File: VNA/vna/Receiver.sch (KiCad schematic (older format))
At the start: 13 parts, among them U5 AD8302ARUZ

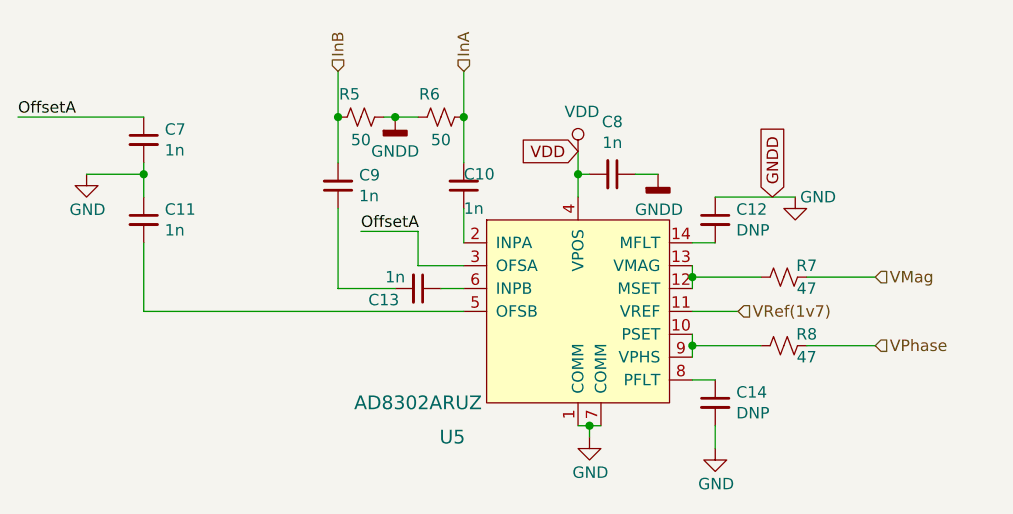
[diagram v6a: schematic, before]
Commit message: initial pcb design
initial layout and grouping of components complete
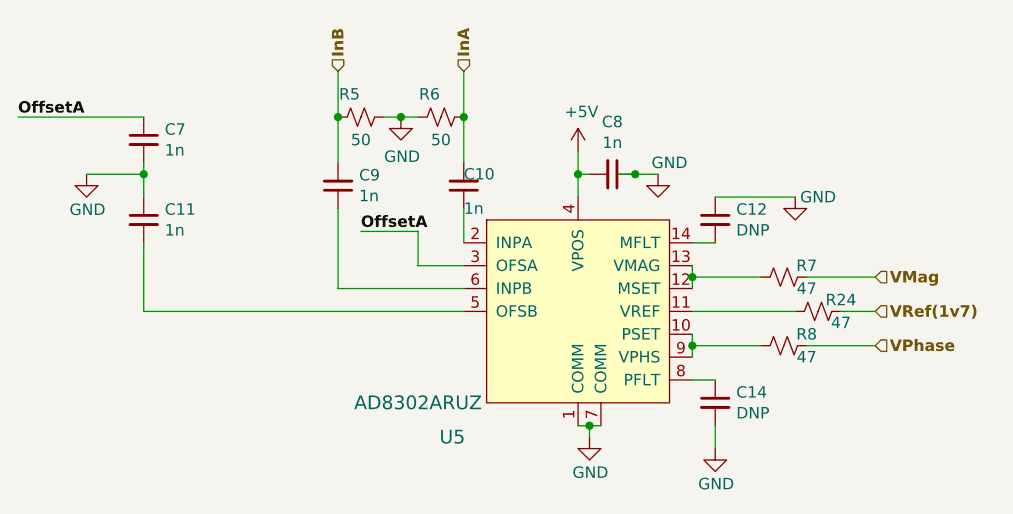
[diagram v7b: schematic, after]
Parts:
- removed C13: 1n, Capacitor_SMD:C_1206_3216Metric_Pad1.42x1.75mm_HandSolder, symbol Device:C_Small
- added R24: 47, Resistor_SMD:R_0805_2012Metric_Pad1.15x1.40mm_HandSolder, symbol Device:R_Small_US
- C10, C11, C12, C14, C7, C8, C9: footprint Capacitor_SMD:C_1206_3216Metric_Pad1.42x1.75mm_HandSolder -> Capacitor_SMD:C_0805_2012Metric_Pad1.15x1.40mm_HandSolder
- R5, R6, R7, R8: footprint Resistor_SMD:R_1206_3216Metric_Pad1.42x1.75mm_HandSolder -> Resistor_SMD:R_0805_2012Metric_Pad1.15x1.40mm_HandSolder
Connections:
- net VRef(1v7): now also R24.1; no longer U5.11 (VREF)
- net at U5.6 (INPB): now also C9.1
- net VDD renamed +5V
- new net: R24.2, U5.11 (VREF)
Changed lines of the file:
@@
 $Descr A4 11693 8268
 encoding utf-8
-Sheet 6 10
-Title ""
-Date ""
-Rev ""
-Comp ""
+Sheet 5 10
+Title "Receiver"
+Date "2019-09-25"
+Rev "0.1"
+Comp "Benjamin Jackson"
 Comment1 ""
 Comment2 ""
@@
 F 0 "C12" H 6142 2796 50  0000 L CNN
 F 1 "DNP" H 6142 2705 50  0000 L CNN
-F 2 "Capacitor_SMD:C_1206_3216Metric_Pad1.42x1.75mm_HandSolder" H 6050 2750 50  0001 C CNN
+F 2 "Capacitor_SMD:C_0805_2012Metric_Pad1.15x1.40mm_HandSolder" H 6050 2750 50  0001 C CNN
 F 3 "~" H 6050 2750 50  0001 C CNN
 	1    6050 2750
@@
 F 0 "C14" H 6142 3596 50  0000 L CNN
 F 1 "DNP" H 6142 3505 50  0000 L CNN
-F 2 "Capacitor_SMD:C_1206_3216Metric_Pad1.42x1.75mm_HandSolder" H 6050 3550 50  0001 C CNN
+F 2 "Capacitor_SMD:C_0805_2012Metric_Pad1.15x1.40mm_HandSolder" H 6050 3550 50  0001 C CNN
 F 3 "~" H 6050 3550 50  0001 C CNN
 	1    6050 3550
@@
 F 0 "C10" H 4950 2550 50  0000 R CNN
 F 1 "1n" H 4950 2700 50  0000 R CNN
-F 2 "Capacitor_SMD:C_1206_3216Metric_Pad1.42x1.75mm_HandSolder" H 4950 2600 50  0001 C CNN
+F 2 "Capacitor_SMD:C_0805_2012Metric_Pad1.15x1.40mm_HandSolder" H 4950 2600 50  0001 C CNN
 F 3 "~" H 4950 2600 50  0001 C CNN
 	1    4950 2600
@@
 Wire Wire Line
 	5950 3450 6050 3450
-$Comp
-L Device:C_Small C13
-U 1 1 5CCC193D
-P 4750 3050
-F 0 "C13" V 4800 2900 50  0000 C CNN
-F 1 "1n" V 4700 2950 50  0000 C CNN
-F 2 "Capacitor_SMD:C_1206_3216Metric_Pad1.42x1.75mm_HandSolder" H 4750 3050 50  0001 C CNN
-F 3 "~" H 4750 3050 50  0001 C CNN
-	1    4750 3050
-	0    1    1    0
-$EndComp
 $Comp
 L power:GND #PWR023
@@
 Wire Wire Line
 	4950 2700 4950 2850
-Text HLabel 4950 2100 1    50   Input ~ 0
+Text HLabel 4950 2100 1    50   Input ~ 10
 InA
 Wire Wire Line
-	4850 3050 4950 3050
-Wire Wire Line
 	4950 2500 4950 2300
-$Comp
-L power:VDD #PWR019
-U 1 1 5CCC3643
-P 5450 2450
-F 0 "#PWR019" H 5450 2300 50  0001 C CNN
-F 1 "VDD" H 5467 2623 50  0000 C CNN
-F 2 "" H 5450 2450 50  0001 C CNN
-F 3 "" H 5450 2450 50  0001 C CNN
-	1    5450 2450
-	1    0    0    -1
-$EndComp
 Wire Wire Line
 	5450 2450 5450 2550
@@
 F 0 "C8" V 5371 2550 50  0000 C CNN
 F 1 "1n" V 5462 2550 50  0000 C CNN
-F 2 "Capacitor_SMD:C_1206_3216Metric_Pad1.42x1.75mm_HandSolder" H 5600 2550 50  0001 C CNN
+F 2 "Capacitor_SMD:C_0805_2012Metric_Pad1.15x1.40mm_HandSolder" H 5600 2550 50  0001 C CNN
 F 3 "~" H 5600 2550 50  0001 C CNN
 	1    5600 2550
@@
 Wire Wire Line
 	5450 2550 5450 2650
-$Comp
-L power:GNDD #PWR021
-U 1 1 5CCC4AF9
-P 5800 2550
-F 0 "#PWR021" H 5800 2300 50  0001 C CNN
-F 1 "GNDD" H 5804 2395 50  0000 C CNN
-F 2 "" H 5800 2550 50  0001 C CNN
-F 3 "" H 5800 2550 50  0001 C CNN
-	1    5800 2550
-	1    0    0    -1
-$EndComp
-Wire Wire Line
-	5700 2550 5800 2550
 $Comp
 L power:GND #PWR022
@@
 Wire Wire Line
 	6050 3650 6050 3750
-Text HLabel 6150 3150 2    50   Input ~ 0
+Text HLabel 6750 3150 2    50   Input ~ 10
 VRef(1v7)
-Wire Wire Line
-	5950 3150 6150 3150
 $Comp
 L Device:R_Small_US R8
@@
 F 0 "R8" V 6300 3400 50  0000 C CNN
 F 1 "47" V 6400 3400 50  0000 C CNN
-F 2 "Resistor_SMD:R_1206_3216Metric_Pad1.42x1.75mm_HandSolder" H 6350 3300 50  0001 C CNN
+F 2 "Resistor_SMD:R_0805_2012Metric_Pad1.15x1.40mm_HandSolder" H 6350 3300 50  0001 C CNN
 F 3 "~" H 6350 3300 50  0001 C CNN
 	1    6350 3300
@@
 Wire Wire Line
 	5950 3300 5950 3350
-Text HLabel 6750 3300 2    50   Input ~ 0
+Text HLabel 6750 3300 2    50   Input ~ 10
 VPhase
 Wire Wire Line
@@
 F 0 "R7" V 6300 3100 50  0000 C CNN
 F 1 "47" V 6400 3100 50  0000 C CNN
-F 2 "Resistor_SMD:R_1206_3216Metric_Pad1.42x1.75mm_HandSolder" H 6350 3000 50  0001 C CNN
+F 2 "Resistor_SMD:R_0805_2012Metric_Pad1.15x1.40mm_HandSolder" H 6350 3000 50  0001 C CNN
 F 3 "~" H 6350 3000 50  0001 C CNN
 	1    6350 3000
 	0    1    1    0
 $EndComp
-Text HLabel 6750 3000 2    50   Input ~ 0
+Text HLabel 6750 3000 2    50   Input ~ 10
 VMag
 Wire Wire Line
@@
 Wire Wire Line
 	5950 3000 5950 3050
-Text HLabel 4400 2100 1    50   Input ~ 0
+Text HLabel 4400 2100 1    50   Input ~ 10
 InB
-Wire Wire Line
-	4650 3050 4400 3050
 $Comp
 L Device:C_Small C9
@@
 F 0 "C9" H 4308 2554 50  0000 R CNN
 F 1 "1n" H 4308 2645 50  0000 R CNN
-F 2 "Capacitor_SMD:C_1206_3216Metric_Pad1.42x1.75mm_HandSolder" H 4400 2600 50  0001 C CNN
+F 2 "Capacitor_SMD:C_0805_2012Metric_Pad1.15x1.40mm_HandSolder" H 4400 2600 50  0001 C CNN
 F 3 "~" H 4400 2600 50  0001 C CNN
 	1    4400 2600
@@
 F 0 "R5" V 4400 2250 50  0000 C CNN
 F 1 "50" V 4600 2300 50  0000 C CNN
-F 2 "Resistor_SMD:R_1206_3216Metric_Pad1.42x1.75mm_HandSolder" H 4500 2300 50  0001 C CNN
+F 2 "Resistor_SMD:R_0805_2012Metric_Pad1.15x1.40mm_HandSolder" H 4500 2300 50  0001 C CNN
 F 3 "~" H 4500 2300 50  0001 C CNN
 	1    4500 2300
@@
 F 0 "R6" V 4750 2250 50  0000 C CNN
 F 1 "50" V 4950 2300 50  0000 C CNN
-F 2 "Resistor_SMD:R_1206_3216Metric_Pad1.42x1.75mm_HandSolder" H 4850 2300 50  0001 C CNN
+F 2 "Resistor_SMD:R_0805_2012Metric_Pad1.15x1.40mm_HandSolder" H 4850 2300 50  0001 C CNN
 F 3 "~" H 4850 2300 50  0001 C CNN
 	1    4850 2300
@@
 Wire Wire Line
 	4950 2300 4950 2100
-$Comp
-L power:GNDD #PWR018
-U 1 1 5CCCF1A1
-P 4650 2300
-F 0 "#PWR018" H 4650 2050 50  0001 C CNN
-F 1 "GNDD" H 4650 2150 50  0000 C CNN
-F 2 "" H 4650 2300 50  0001 C CNN
-F 3 "" H 4650 2300 50  0001 C CNN
-	1    4650 2300
-	1    0    0    -1
-$EndComp
-Wire Wire Line
-	4600 2300 4650 2300
-Connection ~ 4650 2300
-Wire Wire Line
-	4650 2300 4750 2300
 Wire Wire Line
 	4950 3150 3550 3150
@@
 F 0 "C11" H 3642 2796 50  0000 L CNN
 F 1 "1n" H 3642 2705 50  0000 L CNN
-F 2 "Capacitor_SMD:C_1206_3216Metric_Pad1.42x1.75mm_HandSolder" H 3550 2750 50  0001 C CNN
+F 2 "Capacitor_SMD:C_0805_2012Metric_Pad1.15x1.40mm_HandSolder" H 3550 2750 50  0001 C CNN
 F 3 "~" H 3550 2750 50  0001 C CNN
 	1    3550 2750
@@
 F 0 "C7" H 3642 2446 50  0000 L CNN
 F 1 "1n" H 3642 2355 50  0000 L CNN
-F 2 "Capacitor_SMD:C_1206_3216Metric_Pad1.42x1.75mm_HandSolder" H 3550 2400 50  0001 C CNN
+F 2 "Capacitor_SMD:C_0805_2012Metric_Pad1.15x1.40mm_HandSolder" H 3550 2400 50  0001 C CNN
 F 3 "~" H 3550 2400 50  0001 C CNN
 	1    3550 2400
@@
 Wire Wire Line
 	4750 2950 4750 2800
-Text Label 3000 2300 0    50   ~ 0
+Text Label 3000 2300 0    50   ~ 10
 OffsetA
 Wire Wire Line
@@
 Wire Wire Line
 	4750 2800 4500 2800
-Text Label 4500 2800 0    50   ~ 0
+Text Label 4500 2800 0    50   ~ 10
 OffsetA
 $Comp
@@
 Wire Wire Line
 	3550 2550 3550 2650
-Text GLabel 5450 2450 0    50   Input ~ 0
-VDD
-Text GLabel 6300 2650 1    50   Input ~ 0
-GNDD
+$Comp
+L power:+5V #PWR0117
+U 1 1 5D8BDDE5
+P 5450 2450
+F 0 "#PWR0117" H 5450 2300 50  0001 C CNN
+F 1 "+5V" H 5465 2623 50  0000 C CNN
+F 2 "" H 5450 2450 50  0001 C CNN
+F 3 "" H 5450 2450 50  0001 C CNN
+	1    5450 2450
+	1    0    0    -1
+$EndComp
+Wire Wire Line
+	4400 3050 4950 3050
+$Comp
+L power:GND #PWR0118
+U 1 1 5D97EF48
+P 4675 2300
+F 0 "#PWR0118" H 4675 2050 50  0001 C CNN
+F 1 "GND" H 4680 2127 50  0000 C CNN
+F 2 "" H 4675 2300 50  0001 C CNN
+F 3 "" H 4675 2300 50  0001 C CNN
+	1    4675 2300
+	1    0    0    -1
+$EndComp
+Wire Wire Line
+	4675 2300 4750 2300
+Wire Wire Line
+	4675 2300 4600 2300
+Connection ~ 4675 2300
+$Comp
+L Device:R_Small_US R24
+U 1 1 5D98FE1B
+P 6500 3150
+F 0 "R24" V 6450 3250 50  0000 C CNN
+F 1 "47" V 6550 3250 50  0000 C CNN
+F 2 "Resistor_SMD:R_0805_2012Metric_Pad1.15x1.40mm_HandSolder" H 6500 3150 50  0001 C CNN
+F 3 "~" H 6500 3150 50  0001 C CNN
+	1    6500 3150
+	0    1    1    0
+$EndComp
+Wire Wire Line
+	6600 3150 6750 3150
+Wire Wire Line
+	5950 3150 6400 3150
+$Comp
+L power:GND #PWR0119
+U 1 1 5D9B97F0
+P 5800 2550
+F 0 "#PWR0119" H 5800 2300 50  0001 C CNN
+F 1 "GND" H 5850 2600 50  0000 C CNN
+F 2 "" H 5800 2550 50  0001 C CNN
+F 3 "" H 5800 2550 50  0001 C CNN
+	1    5800 2550
+	1    0    0    -1
+$EndComp
+Wire Wire Line
+	5625 2550 5700 2550
+Connection ~ 5700 2550
+Wire Wire Line
+	5700 2550 5800 2550
 $EndSCHEMATC
